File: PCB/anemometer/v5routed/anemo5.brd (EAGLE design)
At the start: 100 x 80 mm, 77 parts, among them IC1 AD8223, IC2 AD8223, IC3 AD8223, IC4 AD8223, IC5 TL072D, IC6 TL072D, IC7 TL072D, J1 RJ12STRAIGHT-I2C, J2 RJ12STRAIGHT-I2C

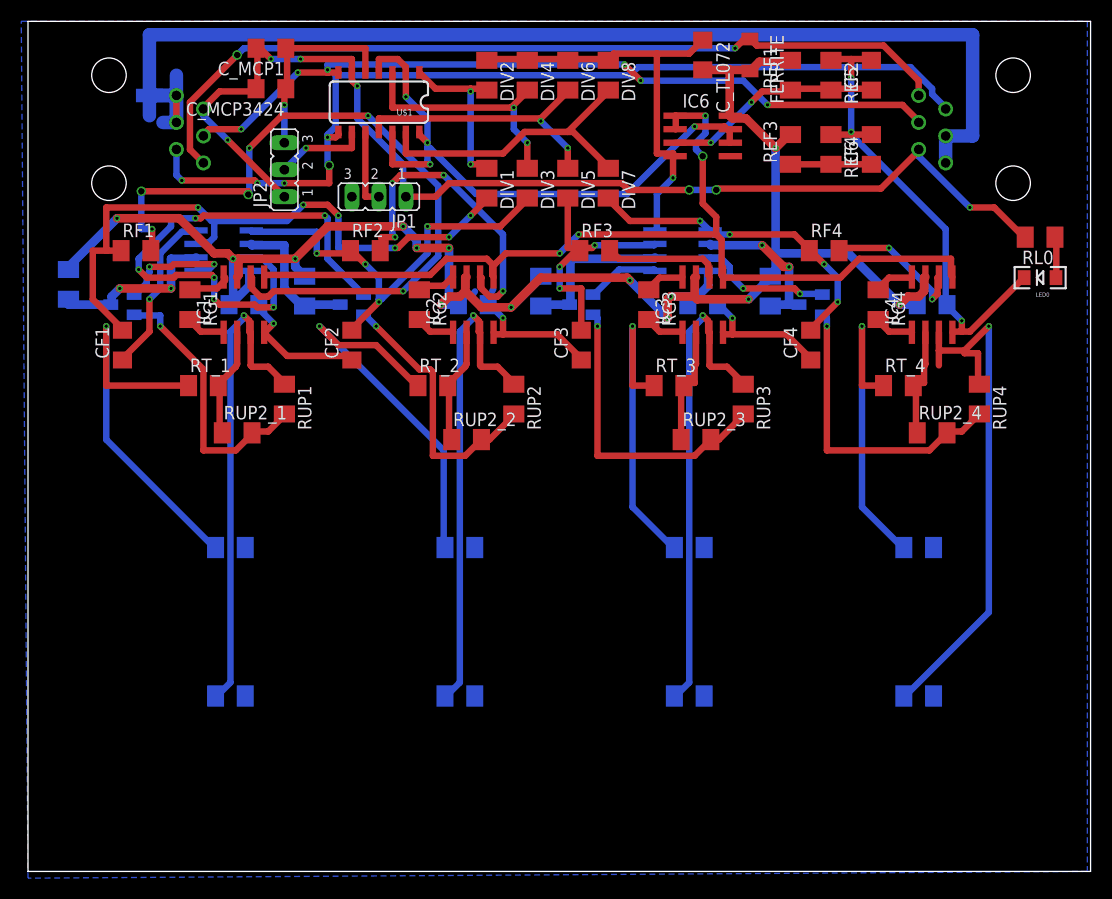
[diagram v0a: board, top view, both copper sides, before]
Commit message: created gerber for anemo5
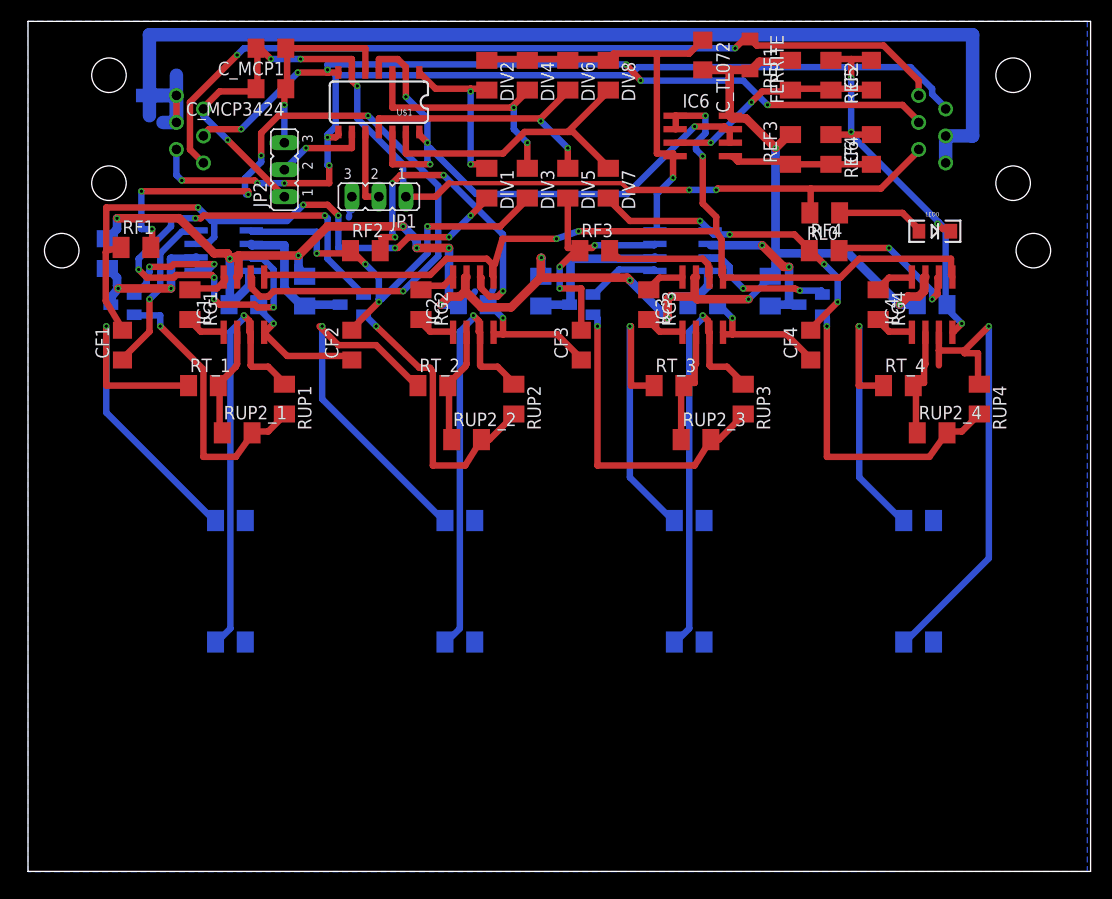
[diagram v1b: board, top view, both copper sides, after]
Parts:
- FERRITE: value 80Ohm -> ferrite
- moved RL0 20.4 mm to (75.0, 62.0)
- moved LED0 10.8 mm to (85.3, 60.2), turned to 0 degrees
- moved PT100_1 5.08 mm to (19.1, 21.6)
- moved PT100_2 5.08 mm to (40.6, 21.6)
- moved PT100_3 5.08 mm to (62.2, 21.6)
- moved PT100_4 5.08 mm to (83.8, 21.6)
- moved RC1 4.67 mm to (7.47, 58.1)
- moved PT1K_1 2.54 mm to (19.1, 33.0)
- moved PT1K_2 2.54 mm to (40.6, 33.0)
- moved PT1K_3 2.54 mm to (62.2, 33.0)
- moved PT1K_4 2.54 mm to (83.8, 33.0)
- moved RF1 0.30 mm to (10.2, 58.7)
- moved RG2 0.15 mm to (37.0, 53.3)
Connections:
- net N$24: now also IC6.5
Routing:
- net 5V: track 110.3 -> 98.8 mm, vias 7 -> 6
- net N$24: track 7.62 -> 13.6 mm
- net IN+1: track 46.0 -> 40.9 mm
- net IN+4: track 51.4 -> 46.4 mm
- net IN+3: track 46.0 -> 40.9 mm
- net IN+2: track 46.0 -> 40.9 mm
- net N$14: track 3.96 -> 8.28 mm
- net GND: track 171.9 -> 167.7 mm, vias 9 -> 10
- net VCC: track 166.1 -> 162.1 mm
- net N$23: track 38.5 -> 36.0 mm
- net N$25: track 37.4 -> 34.9 mm
- net N$27: track 30.1 -> 28.0 mm
- net N$15: track 16.4 -> 14.2 mm
- net N$29: track 30.1 -> 28.1 mm
- net OUT1: track 61.3 -> 59.4 mm
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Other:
- board text added: "Anemometer v5"
- board text removed: "100"
- board text removed: "1000"
